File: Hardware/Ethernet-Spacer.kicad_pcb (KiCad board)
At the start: 2 copper layers, 34 x 34 mm, 14 parts, among them J10 Conn_01x02_Male, J11 Conn_01x02_Male, J3 Conn_01x02_Male, J4 Conn_01x02_Male, J5 Conn_01x02_Male, J6 Conn_01x02_Male, J7 Conn_01x08_Male, J9 QWIIC_Stackable

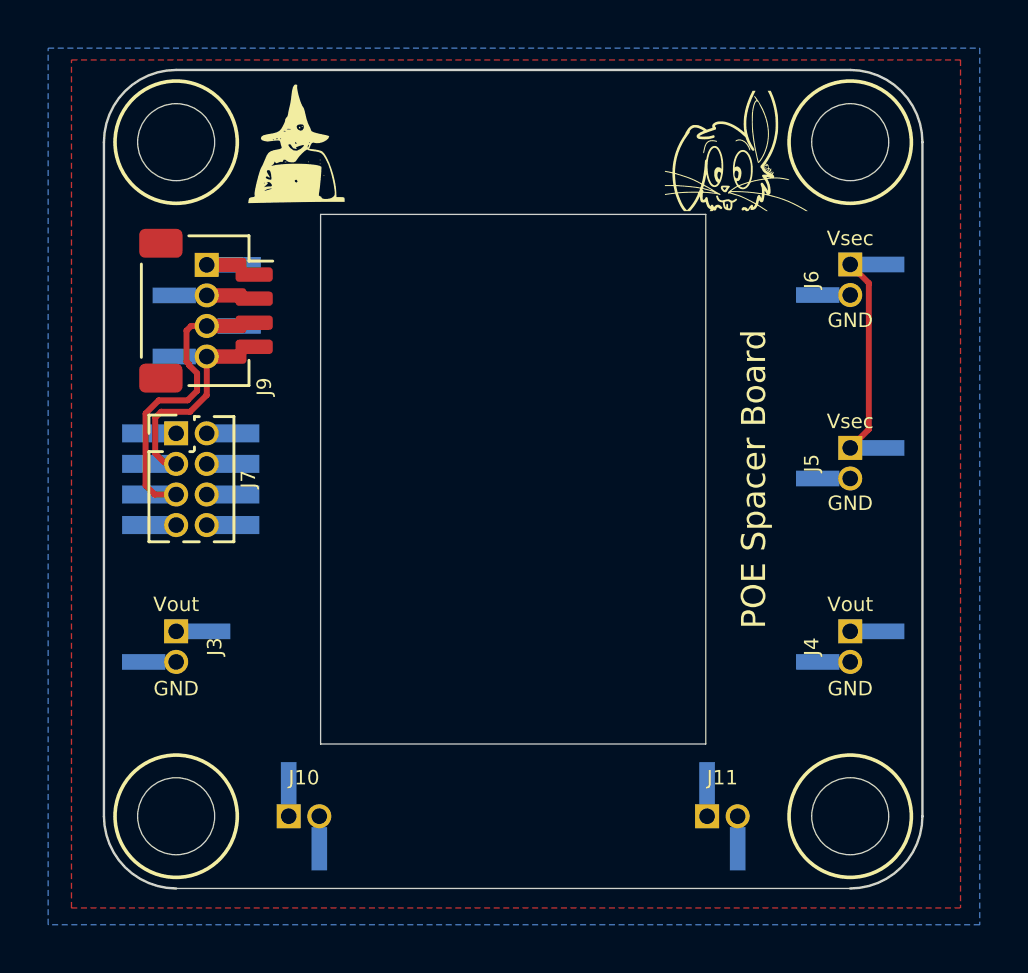
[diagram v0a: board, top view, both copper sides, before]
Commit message: Still working on changes to J7/J9...
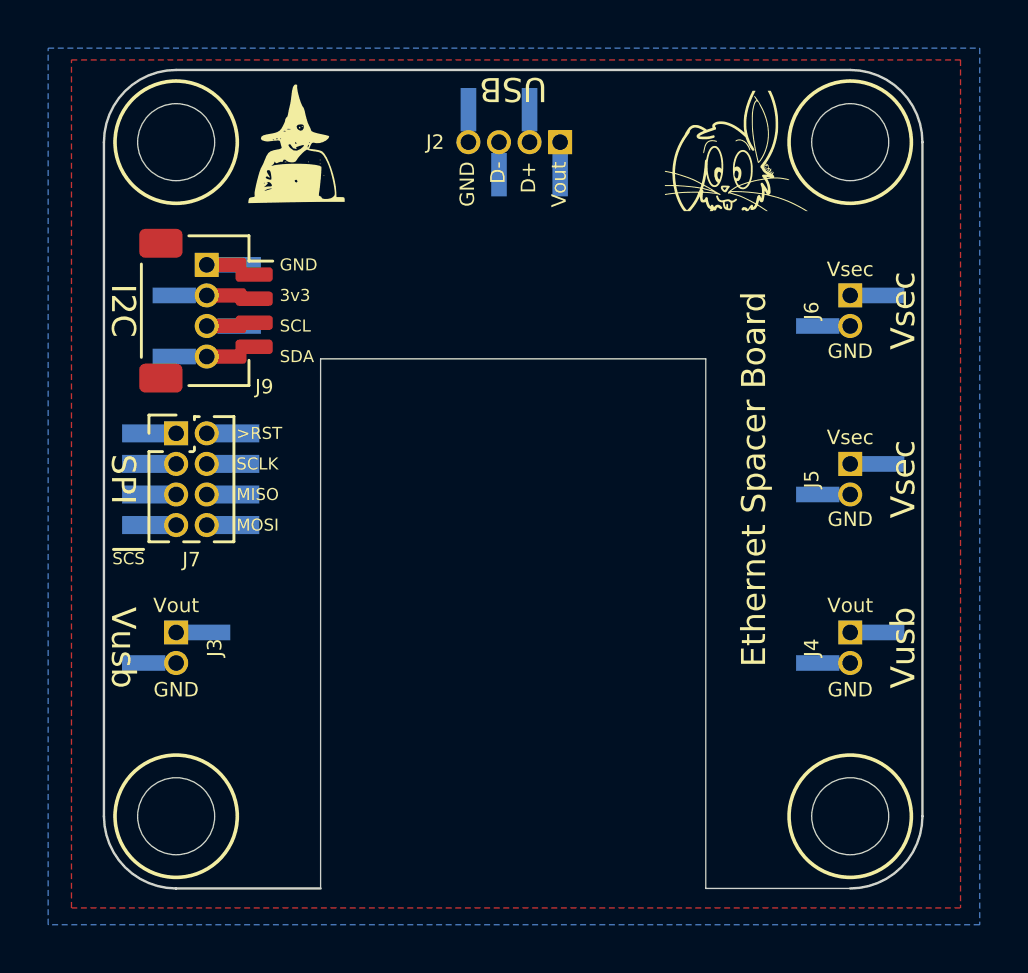
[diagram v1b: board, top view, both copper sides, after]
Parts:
- removed J10, J11: Conn_01x02_Male, Tinker:Board_Stacker_2
- added J2: Conn_01x04_Male, Tinker:Board_Stacker_4, F.Cu at (102.0, 86.0)
- moved J6 1.28 mm to (114.0, 92.4)
- moved J5 0.66 mm to (114.0, 99.4)
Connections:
- net WIZ_RST renamed ~{SCS}3
- J5 pad 1: Vsec -> unconnected-(J5-Pad1)
- J6 pad 1: Vsec -> unconnected-(J6-Pad1)
- J7 pad 2: SCLK -> RESET
- J7 pad 3: SCL -> ~{SCS}2
- J7 pad 4: MISO -> SCLK
- J7 pad 5: SDA -> ~{SCS}1
- J7 pad 6: MOSI -> MISO
- J7 pad 7: unconnected-(J7-Pad7) -> ~{SCS}0
- J7 pad 8: ~{SCS} -> MOSI
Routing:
- net SDA: track 10.6 -> 0.00 mm
- net Vsec: track 8.26 -> 0.00 mm
- net SCL: track 6.15 -> 0.00 mm
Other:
- outline, holes or cut-outs redrawn
- board text added: "3v3"
- board text added: ">RST"
- board text added: "D+"
- board text added: "D-"
- board text added: "MISO"
- board text added: "MOSI"
- board text added: "SCL"
- board text added: "SCLK"
- board text added: "SDA"
- board text added: "SPI"
- board text added: "USB"
- board text added: "Vusb"
- board text added: "~{SCS}"

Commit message: Still migrating to 0.2.x
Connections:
- net ~{SCS}3 renamed ~{RESET}
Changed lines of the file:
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@@
   (net 3 "SDA")
   (net 4 "SCL")
-  (net 5 "~{SCS}3")
+  (net 5 "~{RESET}")
   (net 6 "SCLK")
   (net 7 "MISO")
@@
     (descr "JST SH series connector, SM04B-SRSS-TB (http://www.jst-mfg.com/product/pdf/eng/eSH.pdf), generated with kicad-footprint-generator")
     (tags "connector JST SH top entry")
-    (property "Sheetfile" "Ethernet-S.kicad_sch")
+    (property "Sheetfile" "Ethernet-Spacer.kicad_sch")
     (property "Sheetname" "")
     (property "exclude_from_bom" "")
@@
     (tags "Through hole pin header THT 2x04 1.27mm double row")
     (property "LCSC" "C2881786 + C2684732")
-    (property "Sheetfile" "Ethernet-S.kicad_sch")
+    (property "Sheetfile" "Ethernet-Spacer.kicad_sch")
     (property "Sheetname" "")
     (property "exclude_from_bom" "")
@@
     (fp_line (start -1.07 4.445) (end -1.07 0.2175) (layer "F.Fab") (width 0.1))
     (pad "1" smd rect (at -1.195 0) (size 2.1 0.75) (layers "B.Cu" "B.Paste" "B.Mask")
-      (net 5 "~{SCS}3") (pinfunction "Pin_1") (pintype "passive"))
+      (net 5 "~{RESET}") (pinfunction "Pin_1") (pintype "passive"))
     (pad "1" thru_hole rect (at 0 0) (size 1 1) (drill 0.65) (layers *.Cu *.Mask)
-      (net 5 "~{SCS}3") (pinfunction "Pin_1") (pintype "passive"))
+      (net 5 "~{RESET}") (pinfunction "Pin_1") (pintype "passive"))
     (pad "2" smd rect (at 2.405 0) (size 2.1 0.75) (layers "B.Cu" "B.Paste" "B.Mask")
       (net 9 "RESET") (pinfunction "Pin_2") (pintype "passive"))
@@
     (descr "JST SH series connector, SM04B-SRSS-TB (http://www.jst-mfg.com/product/pdf/eng/eSH.pdf), generated with kicad-footprint-generator")
     (tags "connector JST SH top entry")
-    (property "Sheetfile" "Ethernet-S.kicad_sch")
+    (property "Sheetfile" "Ethernet-Spacer.kicad_sch")
     (property "Sheetname" "")
     (property "exclude_from_bom" "")
@@
     (descr "JST SH series connector, SM04B-SRSS-TB (http://www.jst-mfg.com/product/pdf/eng/eSH.pdf), generated with kicad-footprint-generator")
     (tags "connector JST SH top entry")
-    (property "Sheetfile" "Ethernet-S.kicad_sch")
+    (property "Sheetfile" "Ethernet-Spacer.kicad_sch")
     (property "Sheetname" "")
     (property "exclude_from_bom" "")
@@
     (descr "JST SH series connector, SM04B-SRSS-TB (http://www.jst-mfg.com/product/pdf/eng/eSH.pdf), generated with kicad-footprint-generator")
     (tags "connector JST SH top entry")
-    (property "Sheetfile" "Ethernet-S.kicad_sch")
+    (property "Sheetfile" "Ethernet-Spacer.kicad_sch")
     (property "Sheetname" "")
     (property "exclude_from_bom" "")
@@
     (descr "JST SH series connector, SM04B-SRSS-TB (http://www.jst-mfg.com/product/pdf/eng/eSH.pdf), generated with kicad-footprint-generator")
     (tags "connector JST SH top entry")
-    (property "Sheetfile" "Ethernet-S.kicad_sch")
+    (property "Sheetfile" "Ethernet-Spacer.kicad_sch")
     (property "Sheetname" "")
     (property "exclude_from_bom" "")
@@
     (descr "JST SH series connector, SM04B-SRSS-TB (http://www.jst-mfg.com/product/pdf/eng/eSH.pdf), generated with kicad-footprint-generator")
     (tags "connector JST SH top entry")
-    (property "Sheetfile" "Ethernet-S.kicad_sch")
+    (property "Sheetfile" "Ethernet-Spacer.kicad_sch")
     (property "Sheetname" "")
     (property "exclude_from_bom" "")
